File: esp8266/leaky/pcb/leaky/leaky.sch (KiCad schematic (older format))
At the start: 10 parts, among them Q1 BC327, SW1 sensing loop, U1 DD0405MA

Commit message: leaky: Add ESP8266
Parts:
- added C4: 0.1uF, symbol Device:C_Small
- added J1: UART, symbol _mysyms:UART
- added JP1: PROG, symbol Device:Jumper_NO_Small
- added JP2: STAY_ON, symbol Device:Jumper_NO_Small
- added R4, R5, R6, R7: 10k, symbol Device:R_Small
- added SW2: sensing bot, symbol Switch:SW_SPST
- added TP1, TP2, TP3, TP4, TP5: TestPoint, symbol Connector:TestPoint
- added U2: ESP-12F, symbol ESP8266:ESP-12F
- BT1: value AA batts -> 2xAA
- SW1: value sensing loop -> sensing top
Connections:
- net +3V3: now also C4.1, JP2.1, R4.2, R5.2, R6.2, TP5.1, U2.8 (VCC)
- net EN: now also TP4.1, U2.3 (CH_PD)
- net GND: now also C4.2, J1.4 (GND), JP1.2, R7.2, SW2.1 (A), TP1.1, U2.9 (GND)
- net VBUS: now reaches BT1.1 (+), U1.1 (VI)
- net VBUS: now also J1.1 (3V3), TP2.1
- net at Q1.1 (C), R2.1, R3.2: now also JP2.2, TP3.1
- net at R1.2, SW1.2 (B): now also SW2.2 (B)
- new net IO0: JP1.1, R5.1, U2.12 (GPIO0)
- new net IO15: R7.1, U2.10 (GPIO15)
- new net IO2: R6.1, U2.11 (GPIO2)
- new net RST: R4.1, U2.1 (REST)
- new net RX: J1.2 (TX), U2.15 (RXD)
- new net TX: J1.3 (RX), U2.16 (TXD)
- no-connect marks 0 -> 7
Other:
- moved on the sheet: C3, Q1, R1, R2, R3, SW1

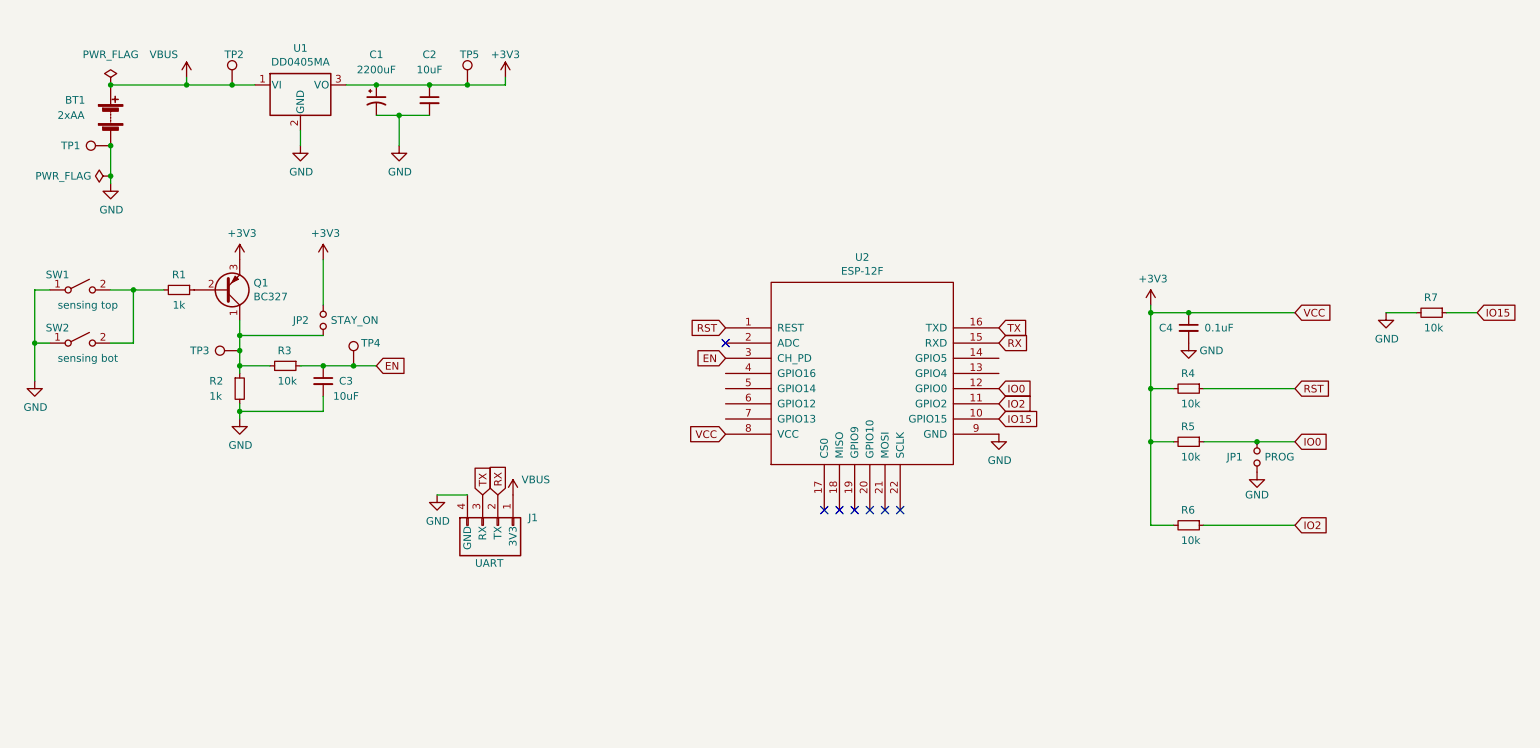
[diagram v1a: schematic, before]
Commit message: leaky: Adjust schematic
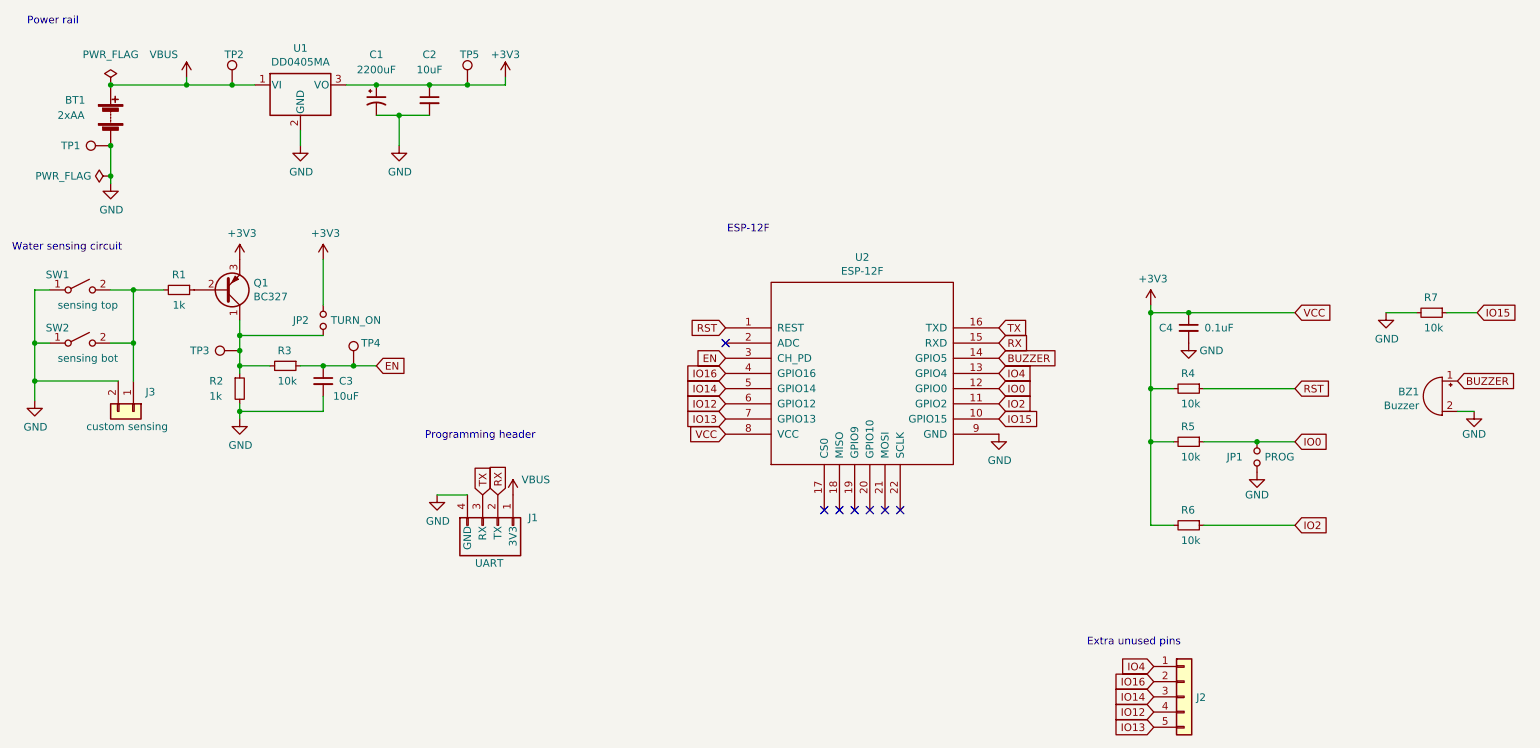
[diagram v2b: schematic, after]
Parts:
- added BZ1: Buzzer, symbol Device:Buzzer
- added J2: extra pins, Connector_PinHeader_2.54mm:PinHeader_1x05_P2.54mm_Vertical, symbol Connector_Generic:Conn_01x05
- added J3: custom sensing, Connector_PinHeader_2.54mm:PinHeader_1x02_P2.54mm_Vertical, symbol Connector_Generic:Conn_01x02
- C2, C3, C4: footprint (none) -> Capacitor_SMD:C_0805_2012Metric_Pad1.18x1.45mm_HandSolder
- J1: footprint (none) -> Connector_PinHeader_2.54mm:PinHeader_1x04_P2.54mm_Vertical
- JP1: footprint (none) -> Connector_PinHeader_2.54mm:PinHeader_1x02_P2.54mm_Vertical
- JP2: value STAY_ON -> TURN_ON; footprint (none) -> Connector_PinHeader_2.54mm:PinHeader_1x02_P2.54mm_Vertical
- R1, R2, R3, R4, R5, R6, R7: footprint (none) -> Resistor_SMD:R_0805_2012Metric_Pad1.15x1.40mm_HandSolder
- TP1, TP2, TP3, TP4, TP5: footprint (none) -> TestPoint:TestPoint_Pad_D1.0mm
- U1: footprint DD0405MA -> (none)
- U2: footprint (none) -> ESP8266:ESP-12E_SMD
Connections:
- net GND: now also BZ1.2 (+), J3.2 (Pin_2)
- net at R1.2, SW1.2 (B), SW2.2 (B): now also J3.1 (Pin_1)
- net IO4: now reaches U2.13 (GPIO4)
- net IO4: now also J2.1 (Pin_1)
- net BUZZER: now reaches U2.14 (GPIO5)
- net BUZZER: now also BZ1.1 (-)
- net IO16: now reaches U2.4 (GPIO16)
- net IO16: now also J2.2 (Pin_2)
- net IO14: now reaches U2.5 (GPIO14)
- net IO14: now also J2.3 (Pin_3)
- net IO12: now reaches U2.6 (GPIO12)
- net IO12: now also J2.4 (Pin_4)
- net IO13: now reaches U2.7 (GPIO13)
- net IO13: now also J2.5 (Pin_5)
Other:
- note added: "ESP-12F"
- note added: "Extra unused pins"
- note added: "Power rail"
- note added: "Programming header"
- note added: "Water sensing circuit\n"
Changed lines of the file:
@@
 F 0 "U1" H 2550 1242 50  0000 C CNN
 F 1 "DD0405MA" H 2550 1151 50  0000 C CNN
-F 2 "DD0405MA" H 2550 1225 50  0001 C CIN
+F 2 "" H 2550 1225 50  0001 C CIN
 F 3 "https://datasheet.lcsc.com/szlcsc/Nanjing-Micro-One-Elec-ME2108A33M3G_C236804.pdf" H 2550 950 50  0001 C CNN
 	1    2550 1000
@@
 F 0 "C2" H 3400 1400 50  0000 C CNN
 F 1 "10uF" H 3400 1300 50  0000 C CNN
-F 2 "" H 3400 1100 50  0001 C CNN
+F 2 "Capacitor_SMD:C_0805_2012Metric_Pad1.18x1.45mm_HandSolder" H 3400 1100 50  0001 C CNN
 F 3 "~" H 3400 1100 50  0001 C CNN
 	1    3400 1100
@@
 F 0 "R1" V 1650 2350 50  0000 C CNN
 F 1 "1k" V 1850 2350 50  0000 C CNN
-F 2 "" H 1750 2350 50  0001 C CNN
+F 2 "Resistor_SMD:R_0805_2012Metric_Pad1.15x1.40mm_HandSolder" H 1750 2350 50  0001 C CNN
 F 3 "~" H 1750 2350 50  0001 C CNN
 	1    1750 2350
@@
 L power:GND #PWR01
 U 1 1 5F793765
-P 800 2950
-F 0 "#PWR01" H 800 2700 50  0001 C CNN
-F 1 "GND" H 805 2777 50  0000 C CNN
-F 2 "" H 800 2950 50  0001 C CNN
-F 3 "" H 800 2950 50  0001 C CNN
-	1    800  2950
+P 800 3080
+F 0 "#PWR01" H 800 2830 50  0001 C CNN
+F 1 "GND" H 805 2907 50  0000 C CNN
+F 2 "" H 800 3080 50  0001 C CNN
+F 3 "" H 800 3080 50  0001 C CNN
+	1    800  3080
 	1    0    0    -1
 $EndComp
@@
 F 0 "R2" H 1950 3050 50  0000 L CNN
 F 1 "1k" H 1950 2950 50  0000 L CNN
-F 2 "" H 2150 3000 50  0001 C CNN
+F 2 "Resistor_SMD:R_0805_2012Metric_Pad1.15x1.40mm_HandSolder" H 2150 3000 50  0001 C CNN
 F 3 "~" H 2150 3000 50  0001 C CNN
 	1    2150 3000
@@
 F 0 "R3" V 2350 2800 50  0000 L CNN
 F 1 "10k" V 2550 2800 50  0000 L CNN
-F 2 "" H 2450 2850 50  0001 C CNN
+F 2 "Resistor_SMD:R_0805_2012Metric_Pad1.15x1.40mm_HandSolder" H 2450 2850 50  0001 C CNN
 F 3 "~" H 2450 2850 50  0001 C CNN
 	1    2450 2850
@@
 F 0 "C3" H 2850 2950 50  0000 C CNN
 F 1 "10uF" H 2850 2850 50  0000 C CNN
-F 2 "" H 2700 2950 50  0001 C CNN
+F 2 "Capacitor_SMD:C_0805_2012Metric_Pad1.18x1.45mm_HandSolder" H 2700 2950 50  0001 C CNN
 F 3 "~" H 2700 2950 50  0001 C CNN
 	1    2700 2950
@@
 	1300 2350 1450 2350
 Wire Wire Line
-	1450 2350 1450 2700
-Wire Wire Line
 	1450 2700 1300 2700
 Connection ~ 1450 2350
@@
 Wire Wire Line
 	800  2700 900  2700
-Wire Wire Line
-	800  2700 800  2950
 Connection ~ 800  2700
 $Comp
@@
 F 0 "U2" H 6250 3665 50  0000 C CNN
 F 1 "ESP-12F" H 6250 3574 50  0000 C CNN
-F 2 "" H 6250 2900 50  0001 C CNN
+F 2 "ESP8266:ESP-12E_SMD" H 6250 2900 50  0001 C CNN
 F 3 "" H 6250 2900 50  0001 C CNN
 	1    6250 2900
@@
 F 0 "C4" H 8250 2600 50  0000 C CNN
 F 1 "0.1uF" H 8600 2600 50  0000 C CNN
-F 2 "" H 8400 2600 50  0001 C CNN
+F 2 "Capacitor_SMD:C_0805_2012Metric_Pad1.18x1.45mm_HandSolder" H 8400 2600 50  0001 C CNN
 F 3 "~" H 8400 2600 50  0001 C CNN
 	1    8400 2600
@@
 F 0 "R4" V 8300 2950 50  0000 L CNN
 F 1 "10k" V 8500 2950 50  0000 L CNN
-F 2 "" H 8400 3000 50  0001 C CNN
+F 2 "Resistor_SMD:R_0805_2012Metric_Pad1.15x1.40mm_HandSolder" H 8400 3000 50  0001 C CNN
 F 3 "~" H 8400 3000 50  0001 C CNN
 	1    8400 3000
@@
 F 0 "R7" V 9900 2450 50  0000 L CNN
 F 1 "10k" V 10100 2450 50  0000 L CNN
-F 2 "" H 10000 2500 50  0001 C CNN
+F 2 "Resistor_SMD:R_0805_2012Metric_Pad1.15x1.40mm_HandSolder" H 10000 2500 50  0001 C CNN
 F 3 "~" H 10000 2500 50  0001 C CNN
 	1    10000 2500
@@
 F 0 "R5" V 8300 3300 50  0000 L CNN
 F 1 "10k" V 8500 3300 50  0000 L CNN
-F 2 "" H 8400 3350 50  0001 C CNN
+F 2 "Resistor_SMD:R_0805_2012Metric_Pad1.15x1.40mm_HandSolder" H 8400 3350 50  0001 C CNN
 F 3 "~" H 8400 3350 50  0001 C CNN
 	1    8400 3350
@@
 F 0 "JP1" V 8850 3250 50  0000 L CNN
 F 1 "PROG" V 8850 3500 50  0000 L CNN
-F 2 "" H 8850 3450 50  0001 C CNN
+F 2 "Connector_PinHeader_2.54mm:PinHeader_1x02_P2.54mm_Vertical" H 8850 3450 50  0001 C CNN
 F 3 "~" H 8850 3450 50  0001 C CNN
 	1    8850 3450
@@
 F 0 "R6" V 8300 3850 50  0000 L CNN
 F 1 "10k" V 8500 3850 50  0000 L CNN
-F 2 "" H 8400 3900 50  0001 C CNN
+F 2 "Resistor_SMD:R_0805_2012Metric_Pad1.15x1.40mm_HandSolder" H 8400 3900 50  0001 C CNN
 F 3 "~" H 8400 3900 50  0001 C CNN
 	1    8400 3900
@@
 F 0 "J1" H 4050 3850 50  0000 L CNN
 F 1 "UART" H 3700 3550 50  0000 L CNN
-F 2 "" V 3850 3800 50  0001 C CNN
+F 2 "Connector_PinHeader_2.54mm:PinHeader_1x04_P2.54mm_Vertical" V 3850 3800 50  0001 C CNN
 F 3 "~" V 3850 3800 50  0001 C CNN
 	1    3800 3850
@@
 P 2700 2550
 F 0 "JP2" V 2700 2350 50  0000 L CNN
-F 1 "STAY_ON" V 2700 2600 50  0000 L CNN
-F 2 "" H 2700 2550 50  0001 C CNN
+F 1 "TURN_ON" V 2700 2600 50  0000 L CNN
+F 2 "Connector_PinHeader_2.54mm:PinHeader_1x02_P2.54mm_Vertical" H 2700 2550 50  0001 C CNN
 F 3 "~" H 2700 2550 50  0001 C CNN
 	1    2700 2550
@@
 F 0 "TP2" H 2050 1200 50  0000 L CNN
 F 1 "TestPoint" H 2158 1027 50  0001 L CNN
-F 2 "" H 2300 1000 50  0001 C CNN
+F 2 "TestPoint:TestPoint_Pad_D1.0mm" H 2300 1000 50  0001 C CNN
 F 3 "~" H 2300 1000 50  0001 C CNN
 	1    2100 1000
@@
 F 0 "TP1" V 1300 1600 50  0000 L CNN
 F 1 "TestPoint" H 1358 1427 50  0001 L CNN
-F 2 "" H 1500 1400 50  0001 C CNN
+F 2 "TestPoint:TestPoint_Pad_D1.0mm" H 1500 1400 50  0001 C CNN
 F 3 "~" H 1500 1400 50  0001 C CNN
 	1    1300 1400
@@
 F 0 "TP5" H 3600 1200 50  0000 L CNN
 F 1 "TestPoint" H 3708 1027 50  0001 L CNN
-F 2 "" H 3850 1000 50  0001 C CNN
+F 2 "TestPoint:TestPoint_Pad_D1.0mm" H 3850 1000 50  0001 C CNN
 F 3 "~" H 3850 1000 50  0001 C CNN
 	1    3650 1000
@@
 F 0 "TP4" H 2950 3000 50  0000 L CNN
 F 1 "TestPoint" H 2958 2877 50  0001 L CNN
-F 2 "" H 3100 2850 50  0001 C CNN
+F 2 "TestPoint:TestPoint_Pad_D1.0mm" H 3100 2850 50  0001 C CNN
 F 3 "~" H 3100 2850 50  0001 C CNN
 	1    2900 2850
@@
 F 0 "TP3" V 2150 2950 50  0000 L CNN
 F 1 "TestPoint" H 2208 2777 50  0001 L CNN
-F 2 "" H 2350 2750 50  0001 C CNN
+F 2 "TestPoint:TestPoint_Pad_D1.0mm" H 2350 2750 50  0001 C CNN
 F 3 "~" H 2350 2750 50  0001 C CNN
 	1    2150 2750
@@
 Wire Wire Line
 	1800 950  1800 1000
+$Comp
+L Device:Buzzer BZ1
+U 1 1 5F8AB6F2
+P 10070 3050
+F 0 "BZ1" H 10222 3079 50  0000 L CNN
+F 1 "Buzzer" H 10222 2988 50  0000 L CNN
+F 2 "" V 10045 3150 50  0001 C CNN
+F 3 "~" V 10045 3150 50  0001 C CNN
+	1    10070 3050
+	-1   0    0    -1
+$EndComp
+$Comp
+L power:GND #PWR0106
+U 1 1 5F8AEDDD
+P 10280 3150
+F 0 "#PWR0106" H 10280 2900 50  0001 C CNN
+F 1 "GND" H 10280 3000 50  0000 C CNN
+F 2 "" H 10280 3150 50  0001 C CNN
+F 3 "" H 10280 3150 50  0001 C CNN
+	1    10280 3150
+	-1   0    0    -1
+$EndComp
+Wire Wire Line
+	10170 3150 10280 3150
+Text Notes 750  610  0    50   ~ 0
+Power rail
+Text Notes 5360 1980 0    50   ~ 0
+ESP-12F
+Text Notes 650  2100 0    50   ~ 0
+Water sensing circuit\n
+Text Notes 3370 3340 0    50   ~ 0
+Programming header
+Text Notes 7730 4700 0    50   ~ 0
+Extra unused pins
+Text GLabel 7150 2800 2    50   Input ~ 0
+BUZZER
+Text GLabel 10170 2950 2    50   Input ~ 0
+BUZZER
+$Comp
+L Connector_Generic:Conn_01x05 J2
+U 1 1 5F8BE4F7
+P 8370 5030
+F 0 "J2" H 8450 5026 50  0000 L CNN
+F 1 "extra pins" H 8450 4981 50  0001 L CNN
+F 2 "Connector_PinHeader_2.54mm:PinHeader_1x05_P2.54mm_Vertical" H 8370 5030 50  0001 C CNN
+F 3 "~" H 8370 5030 50  0001 C CNN
+	1    8370 5030
+	1    0    0    -1
+$EndComp
+Text GLabel 7150 2900 2    50   Input ~ 0
+IO4
+Text GLabel 8170 4830 0    50   Input ~ 0
+IO4
+Text GLabel 5350 2900 0    50   Input ~ 0
+IO16
+Text GLabel 8170 4930 0    50   Input ~ 0
+IO16
+Text GLabel 5350 3000 0    50   Input ~ 0
+IO14
+Text GLabel 5350 3100 0    50   Input ~ 0
+IO12
+Text GLabel 5350 3200 0    50   Input ~ 0
+IO13
+Text GLabel 8170 5030 0    50   Input ~ 0
+IO14
+Text GLabel 8170 5130 0    50   Input ~ 0
+IO12
+Text GLabel 8170 5230 0    50   Input ~ 0
+IO13
+$Comp
+L Connector_Generic:Conn_01x02 J3
+U 1 1 5F8C3AD5
+P 1450 3150
+F 0 "J3" V 1322 3230 50  0000 L CNN
+F 1 "custom sensing" V 1550 2840 50  0000 L CNN
+F 2 "Connector_PinHeader_2.54mm:PinHeader_1x02_P2.54mm_Vertical" H 1450 3150 50  0001 C CNN
+F 3 "~" H 1450 3150 50  0001 C CNN
+	1    1450 3150
+	0    1    1    0
+$EndComp
+Wire Wire Line
+	1450 2350 1450 2700
+Connection ~ 1450 2700
+Wire Wire Line
+	1450 2700 1450 2950
+Wire Wire Line
+	800  2700 800  2950
+Wire Wire Line
+	1350 2950 800  2950
+Connection ~ 800  2950
+Wire Wire Line
+	800  2950 800  3080
 $EndSCHEMATC

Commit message: leaky: Add footprints
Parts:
- removed J3: custom sensing, Connector_PinHeader_2.54mm:PinHeader_1x02_P2.54mm_Vertical, symbol Connector_Generic:Conn_01x02
- added H1, H2, H3, H4: MountingHole, MountingHole:MountingHole_3.2mm_M3, symbol Mechanical:MountingHole
- BT1: footprint (none) -> Battery:BatteryHolder_Keystone_2462_2xAA
- SW1, SW2: footprint (none) -> Connector_PinHeader_2.54mm:PinHeader_1x02_P2.54mm_Vertical
- U1: footprint (none) -> _my:DD0405MA
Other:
- note added: "Mounting holes"
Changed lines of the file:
@@
 F 0 "BT1" H 1000 1300 50  0000 L CNN
 F 1 "2xAA" H 950 1200 50  0000 L CNN
-F 2 "" V 1300 1260 50  0001 C CNN
+F 2 "Battery:BatteryHolder_Keystone_2462_2xAA" V 1300 1260 50  0001 C CNN
 F 3 "~" V 1300 1260 50  0001 C CNN
 	1    1300 1200
@@
 F 0 "U1" H 2550 1242 50  0000 C CNN
 F 1 "DD0405MA" H 2550 1151 50  0000 C CNN
-F 2 "" H 2550 1225 50  0001 C CIN
+F 2 "_my:DD0405MA" H 2550 1225 50  0001 C CIN
 F 3 "https://datasheet.lcsc.com/szlcsc/Nanjing-Micro-One-Elec-ME2108A33M3G_C236804.pdf" H 2550 950 50  0001 C CNN
 	1    2550 1000
@@
 F 0 "SW1" H 950 2450 50  0000 C CNN
 F 1 "sensing top" H 1150 2250 50  0000 C CNN
-F 2 "" H 1100 2350 50  0001 C CNN
+F 2 "Connector_PinHeader_2.54mm:PinHeader_1x02_P2.54mm_Vertical" H 1100 2350 50  0001 C CNN
 F 3 "~" H 1100 2350 50  0001 C CNN
 	1    1100 2350
@@
 F 0 "SW2" H 950 2800 50  0000 C CNN
 F 1 "sensing bot" H 1150 2600 50  0000 C CNN
-F 2 "" H 1100 2700 50  0001 C CNN
+F 2 "Connector_PinHeader_2.54mm:PinHeader_1x02_P2.54mm_Vertical" H 1100 2700 50  0001 C CNN
 F 3 "~" H 1100 2700 50  0001 C CNN
 	1    1100 2700
@@
 Text GLabel 8170 5230 0    50   Input ~ 0
 IO13
-$Comp
-L Connector_Generic:Conn_01x02 J3
-U 1 1 5F8C3AD5
-P 1450 3150
-F 0 "J3" V 1322 3230 50  0000 L CNN
-F 1 "custom sensing" V 1550 2840 50  0000 L CNN
-F 2 "Connector_PinHeader_2.54mm:PinHeader_1x02_P2.54mm_Vertical" H 1450 3150 50  0001 C CNN
-F 3 "~" H 1450 3150 50  0001 C CNN
-	1    1450 3150
-	0    1    1    0
-$EndComp
 Wire Wire Line
 	1450 2350 1450 2700
-Connection ~ 1450 2700
-Wire Wire Line
-	1450 2700 1450 2950
-Wire Wire Line
-	800  2700 800  2950
-Wire Wire Line
-	1350 2950 800  2950
-Connection ~ 800  2950
-Wire Wire Line
-	800  2950 800  3080
+$Comp
+L Mechanical:MountingHole H1
+U 1 1 5F8C0139
+P 840 4380
+F 0 "H1" H 940 4380 50  0000 L CNN
+F 1 "MountingHole" H 940 4335 50  0001 L CNN
+F 2 "MountingHole:MountingHole_3.2mm_M3" H 840 4380 50  0001 C CNN
+F 3 "~" H 840 4380 50  0001 C CNN
+	1    840  4380
+	1    0    0    -1
+$EndComp
+$Comp
+L Mechanical:MountingHole H2
+U 1 1 5F8C0FC6
+P 840 4630
+F 0 "H2" H 940 4630 50  0000 L CNN
+F 1 "MountingHole" H 940 4585 50  0001 L CNN
+F 2 "MountingHole:MountingHole_3.2mm_M3" H 840 4630 50  0001 C CNN
+F 3 "~" H 840 4630 50  0001 C CNN
+	1    840  4630
+	1    0    0    -1
+$EndComp
+$Comp
+L Mechanical:MountingHole H3
+U 1 1 5F8C125F
+P 1200 4390
+F 0 "H3" H 1300 4390 50  0000 L CNN
+F 1 "MountingHole" H 1300 4345 50  0001 L CNN
+F 2 "MountingHole:MountingHole_3.2mm_M3" H 1200 4390 50  0001 C CNN
+F 3 "~" H 1200 4390 50  0001 C CNN
+	1    1200 4390
+	1    0    0    -1
+$EndComp
+$Comp
+L Mechanical:MountingHole H4
+U 1 1 5F8C1794
+P 1200 4640
+F 0 "H4" H 1300 4640 50  0000 L CNN
+F 1 "MountingHole" H 1300 4595 50  0001 L CNN
+F 2 "MountingHole:MountingHole_3.2mm_M3" H 1200 4640 50  0001 C CNN
+F 3 "~" H 1200 4640 50  0001 C CNN
+	1    1200 4640
+	1    0    0    -1
+$EndComp
+Text Notes 780  4080 0    50   ~ 0
+Mounting holes
+Wire Wire Line
+	800  2700 800  3080
 $EndSCHEMATC

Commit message: Assign more footprints
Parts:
- BZ1: footprint (none) -> Buzzer_Beeper:Buzzer_12x9.5RM7.6
- C1: footprint (none) -> Capacitor_THT:CP_Radial_D10.0mm_P5.00mm
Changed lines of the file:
@@
 F 0 "C1" H 3050 1400 50  0000 C CNN
 F 1 "2200uF" H 3050 1300 50  0000 C CNN
-F 2 "" H 3050 1100 50  0001 C CNN
+F 2 "Capacitor_THT:CP_Radial_D10.0mm_P5.00mm" H 3050 1100 50  0001 C CNN
 F 3 "~" H 3050 1100 50  0001 C CNN
 	1    3050 1100
@@
 F 0 "BZ1" H 10222 3079 50  0000 L CNN
 F 1 "Buzzer" H 10222 2988 50  0000 L CNN
-F 2 "" V 10045 3150 50  0001 C CNN
+F 2 "Buzzer_Beeper:Buzzer_12x9.5RM7.6" V 10045 3150 50  0001 C CNN
 F 3 "~" V 10045 3150 50  0001 C CNN
 	1    10070 3050

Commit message: leaky" Adjust footprint
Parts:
- U2: footprint ESP8266:ESP-12E_SMD -> _my:ESP-12E_SMD; symbol ESP8266:ESP-12F -> _mysyms:ESP-12F
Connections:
- no-connect marks 7 -> 1
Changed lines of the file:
@@
 Connection ~ 800  2700
-$Comp
-L ESP8266:ESP-12F U2
-U 1 1 5F7A8628
-P 6250 2900
-F 0 "U2" H 6250 3665 50  0000 C CNN
-F 1 "ESP-12F" H 6250 3574 50  0000 C CNN
-F 2 "ESP8266:ESP-12E_SMD" H 6250 2900 50  0001 C CNN
-F 3 "" H 6250 2900 50  0001 C CNN
-	1    6250 2900
-	1    0    0    -1
-$EndComp
-NoConn ~ 6000 3800
-NoConn ~ 6100 3800
-NoConn ~ 6200 3800
-NoConn ~ 6300 3800
-NoConn ~ 6500 3800
 $Comp
 L power:+3V3 #PWR07
@@
 Wire Wire Line
 	1800 1000 2100 1000
-NoConn ~ 6400 3800
 $Comp
 L Device:Jumper_NO_Small JP2
@@
 Wire Wire Line
 	800  2700 800  3080
+$Comp
+L _mysyms:ESP-12F U2
+U 1 1 5F7A8628
+P 6250 2900
+F 0 "U2" H 6250 3665 50  0000 C CNN
+F 1 "ESP-12F" H 6250 3574 50  0000 C CNN
+F 2 "_my:ESP-12E_SMD" H 6250 2900 50  0001 C CNN
+F 3 "" H 6250 2900 50  0001 C CNN
+	1    6250 2900
+	1    0    0    -1
+$EndComp
 $EndSCHEMATC

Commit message: leaky: Add description
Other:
- note added: "VBUS voltage has to be 3V3, not 5V!\nIf you provide power through VBUS, remove batteries first.\nTo flash program: \n 1. Short jumper PROG\n 2. Connect UART\n 3. Short jumper TURN_ON\n"
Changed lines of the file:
@@
 Text Notes 750  610  0    50   ~ 0
 Power rail
-Text Notes 5360 1980 0    50   ~ 0
+Text Notes 5160 1980 0    50   ~ 0
 ESP-12F
 Text Notes 650  2100 0    50   ~ 0
@@
 	1    0    0    -1
 $EndComp
+Text Notes 5120 4400 0    50   ~ 0
+VBUS voltage has to be 3V3, not 5V!\nIf you provide power through VBUS, remove batteries first.\nTo flash program: \n  1. Short jumper PROG\n  2. Connect UART\n  3. Short jumper TURN_ON\n
 $EndSCHEMATC

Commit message: leaky: More reposition
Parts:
- J2: footprint Connector_PinHeader_2.54mm:PinHeader_1x05_P2.54mm_Vertical -> _my:PinHeader_1x05_P2.54mm_Vertical
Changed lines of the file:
@@
 F 0 "J2" H 8450 5026 50  0000 L CNN
 F 1 "extra pins" H 8450 4981 50  0001 L CNN
-F 2 "Connector_PinHeader_2.54mm:PinHeader_1x05_P2.54mm_Vertical" H 8370 5030 50  0001 C CNN
+F 2 "_my:PinHeader_1x05_P2.54mm_Vertical" H 8370 5030 50  0001 C CNN
 F 3 "~" H 8370 5030 50  0001 C CNN
 	1    8370 5030
